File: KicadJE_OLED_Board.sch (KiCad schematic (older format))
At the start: 21 parts

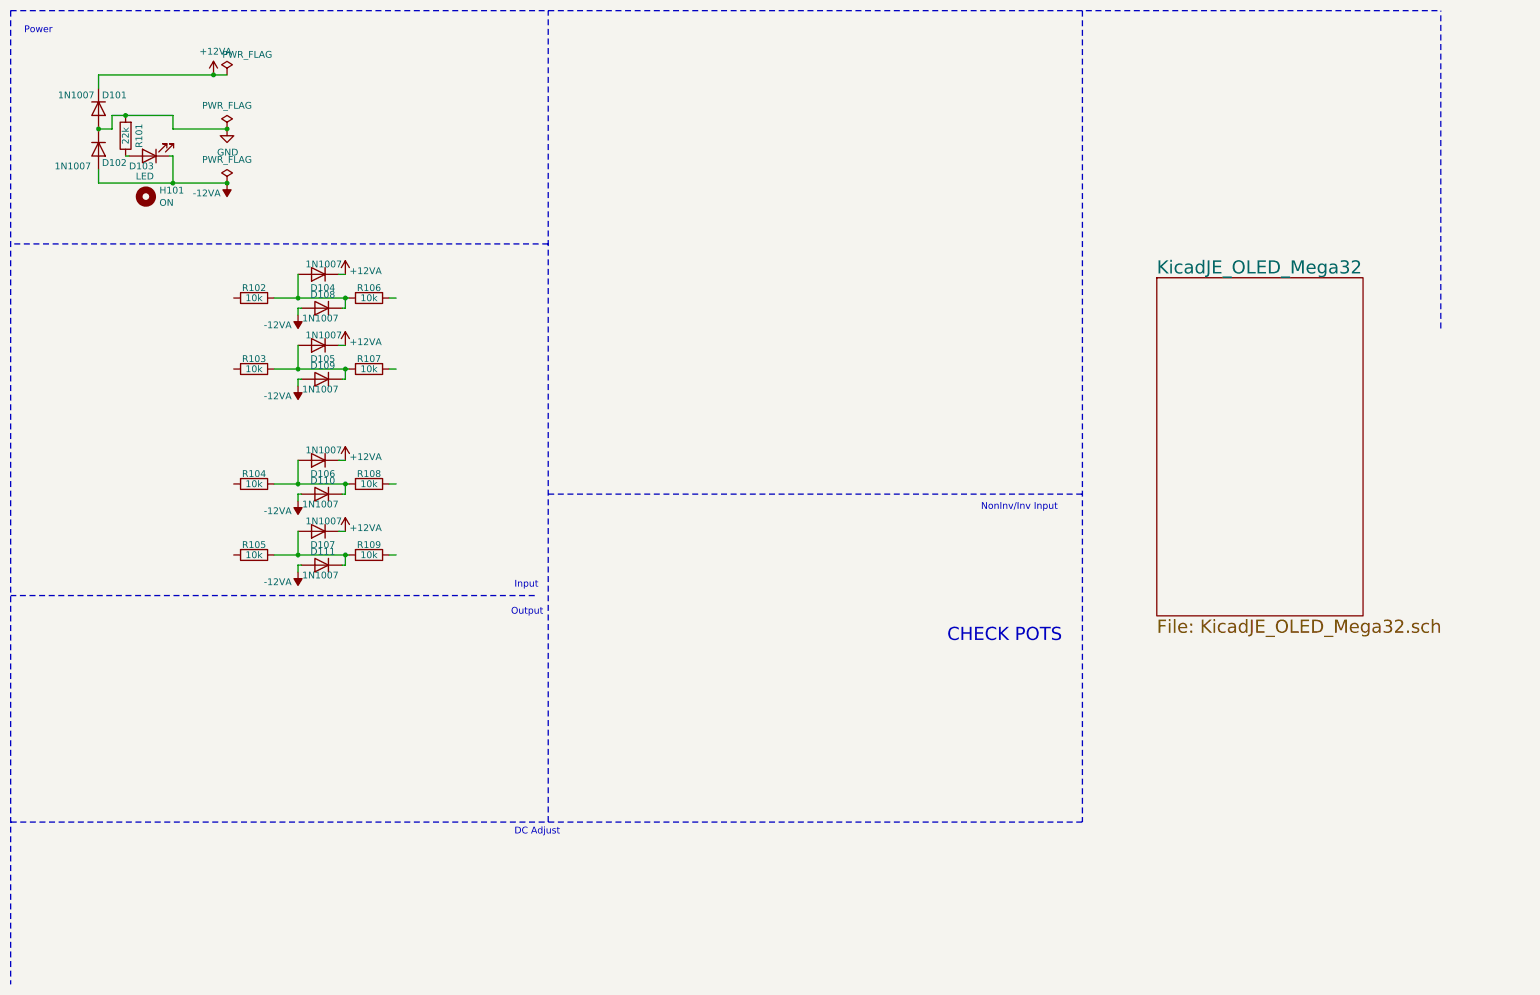
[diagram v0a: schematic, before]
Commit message: Small Amp/Filter circuit
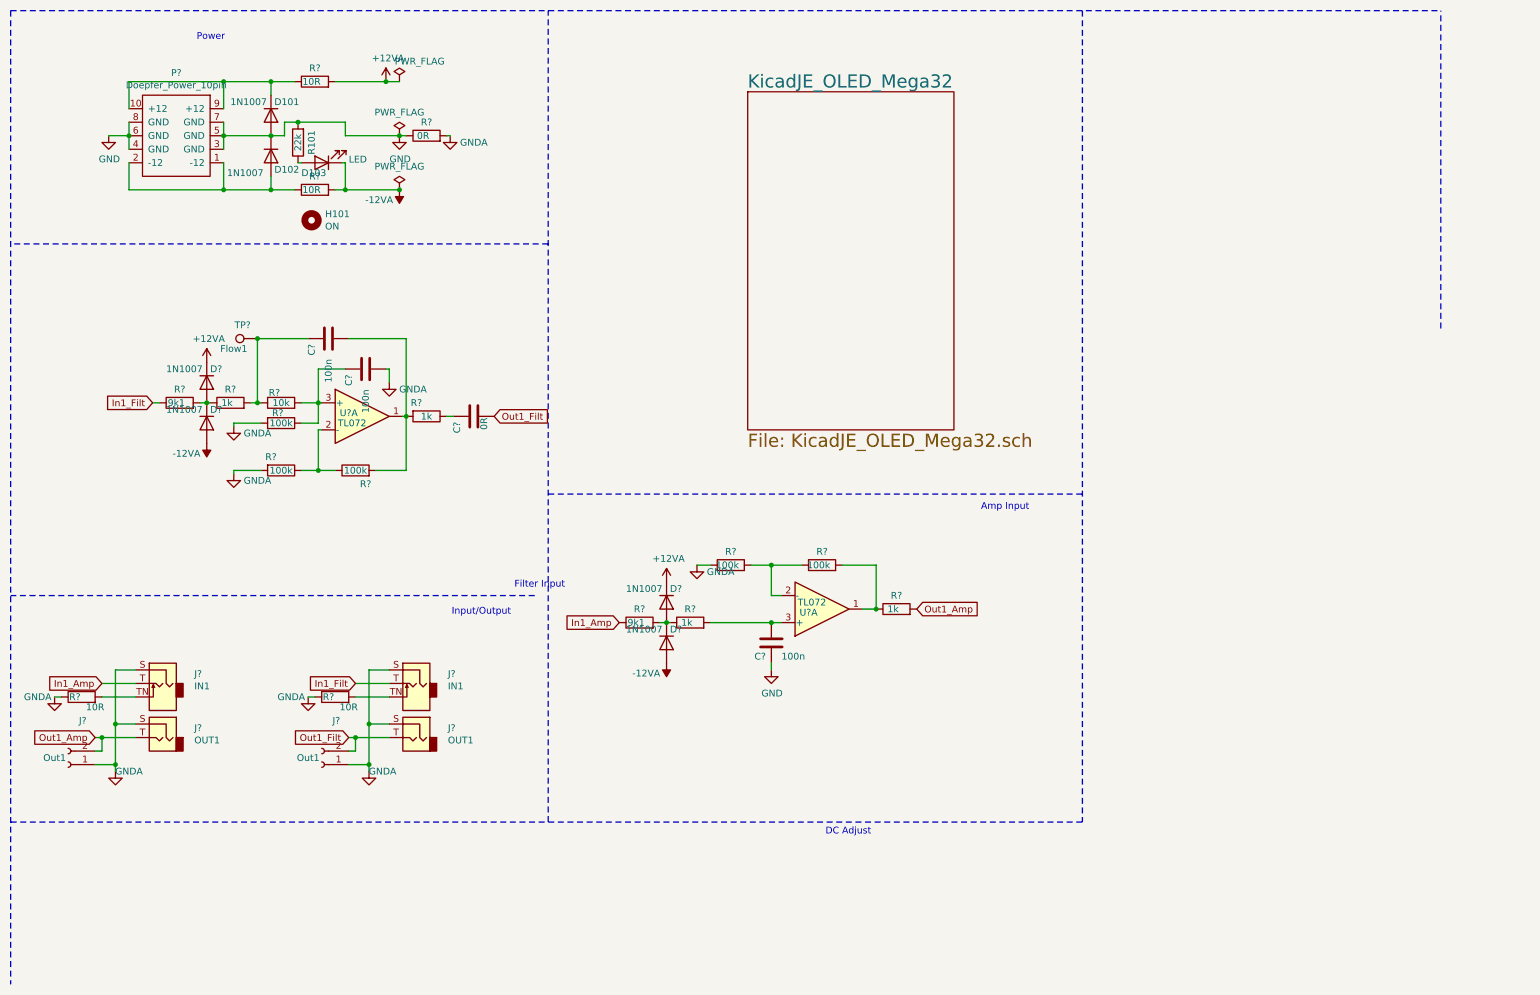
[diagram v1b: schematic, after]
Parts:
- removed D104, D105, D106, D107, D108, D109, D110, D111: 1N1007, AJ:D_SOD-123, symbol Device:D
- removed R102, R103, R104, R105, R106, R107, R108, R109: 10k, AJ:R_0805_AJ, symbol Device:R
- added C? (x3): 100n, AJ:C_0805_AJ, symbol Device:C
- added C?: 0R, AJ:C_0805_AJ, symbol Device:C
- added D? (x4): 1N1007, Diode_SMD:D_SOD-123, symbol Device:D
- added J? (x2): IN1, AJ:PJ301SM, symbol Connector:AudioJack2_SwitchT
- added J? (x2): OUT1, AJ:PJ301SM, symbol Connector:AudioJack2
- added J? (x2): Out1, Connector_PinSocket_2.54mm:PinSocket_1x02_P2.54mm_Vertical, symbol Connector:Conn_01x02_Female
- added P?: Doepfer_Power_10pin, Connectors_IDC:IDC-Header_2x05_Pitch2.54mm_Straight, symbol Eurorack:Doepfer_Power_10pin
- added R? (x4): 1k, AJ:R_0805_AJ, symbol Device:R
- added R? (x5): 100k, AJ:R_0805_AJ, symbol Device:R
- added R?: 10k, AJ:R_0805_AJ, symbol Device:R
- added R? (x4): 10R, AJ:R_0805_AJ, symbol Device:R
- added R? (x2): 9k1, AJ:R_0805_AJ, symbol Device:R
- added R?: 0R, AJ:R_0805_AJ, symbol Device:R
- added TP?: Flow1, TestPoint:TestPoint_THTPad_1.0x1.0mm_Drill0.5mm, symbol Connector:TestPoint
- added U? (x2): TL072, AJ:AJ_SO-8_5.3x6.2mm_P1.27mm, symbol Amplifier_Operational:TL072
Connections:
- net labels added: GNDA, In1_Amp, In1_Filt, Out1_Amp, Out1_Filt
- wire segments 55 -> 101
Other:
- note added: "Amp Input"
- note added: "Filter Input"
- note added: "Input/Output"
- note removed: "CHECK POTS"
- note removed: "Input"
- note removed: "NonInv/Inv Input"
- note removed: "Output"
- moved on the sheet: D101, D102, D103, H101, R101

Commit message: Update KicadJE_OLED_Board.sch
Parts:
- gave numbers to parts that had none: 35

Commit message: Update KicadJE_OLED_Board.sch
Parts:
- added C105, C106: 100n, AJ:C_0805_AJ, symbol Device:C
- added unit 3 of U101
- P101: footprint Connectors_IDC:IDC-Header_2x05_Pitch2.54mm_Straight -> Connector_IDC:IDC-Header_2x05_P2.54mm_Vertical
- renumbered U102 to U101
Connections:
- net +12VA: now also C105.1, U101.8 (V+)
- net -12VA: now also C106.2, U101.4 (V-)
- net GND: now also C105.2, C106.1
- net at R117.2, R118.1: now also U101.7; no longer U101.1
- net at R116.2, R117.1: now also U101.6 (-); no longer U101.2 (-)
- net at C104.1, R115.2: now also U101.5 (+); no longer U101.3 (+)
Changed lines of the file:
@@
 $EndComp
 Wire Wire Line
-	3000 1450 3400 1450
-Wire Wire Line
-	3000 1850 3400 1850
+	3000 1450 3175 1450
+Wire Wire Line
+	3000 1850 3175 1850
 Wire Wire Line
 	2450 1850 2625 1850
@@
 $Comp
 L Amplifier_Operational:TL072 U?
-U 1 1 6221EBDA
+U 2 1 6221EBDA
 P 6525 4950
 AR Path="/5D99B81E/6221EBDA" Ref="U?"  Part="3"
@@
 AR Path="/5E62ACA1/6221EBDA" Ref="U?"  Part="1"
 AR Path="/5F49A670/6221EBDA" Ref="U?"  Part="1"
-AR Path="/6221EBDA" Ref="U102"  Part="1"
+AR Path="/6221EBDA" Ref="U101"  Part="2"
 AR Path="/608CA457/6221EBDA" Ref="U?"  Part="2"
-F 0 "U102" H 6425 4975 50  0000 C CNN
+F 0 "U101" H 6425 4975 50  0000 C CNN
 F 1 "TL072" H 6450 4900 50  0000 C CNN
 F 2 "AJ:AJ_SO-8_5.3x6.2mm_P1.27mm" H 6525 4950 50  0001 C CNN
 F 3 "http://www.ti.com/lit/ds/symlink/tl071.pdf" H 6525 4950 50  0001 C CNN
-	1    6525 4950
+	2    6525 4950
 	1    0    0    1
 $EndComp
@@
 F 0 "P101" H 1750 985 50  0000 C CNN
 F 1 "Doepfer_Power_10pin" H 1750 1076 50  0000 C CNN
-F 2 "Connectors_IDC:IDC-Header_2x05_Pitch2.54mm_Straight" H 1750 1350 50  0001 C CNN
+F 2 "Connector_IDC:IDC-Header_2x05_P2.54mm_Vertical" H 1750 1350 50  0001 C CNN
 F 3 "DOCUMENTATION" H 1750 1350 50  0001 C CNN
 	1    1750 1350
@@
 $EndComp
 Wire Wire Line
-	2925 1050 3300 1050
+	2925 1050 3175 1050
 $Comp
 L Device:R R109
@@
 Wire Wire Line
 	2925 1850 3000 1850
+$Comp
+L Amplifier_Operational:TL072 U?
+U 3 1 6229AF2C
+P 4400 1450
+AR Path="/5D99B81E/6229AF2C" Ref="U?"  Part="3"
+AR Path="/5D99B7BA/6229AF2C" Ref="U?"  Part="1"
+AR Path="/5F18E4B5/6229AF2C" Ref="U?"  Part="2"
+AR Path="/5E62ACA1/6229AF2C" Ref="U?"  Part="1"
+AR Path="/5F49A670/6229AF2C" Ref="U?"  Part="1"
+AR Path="/6229AF2C" Ref="U101"  Part="3"
+AR Path="/608CA457/6229AF2C" Ref="U?"  Part="1"
+F 0 "U101" H 4300 1475 50  0000 C CNN
+F 1 "TL072" H 4325 1400 50  0000 C CNN
+F 2 "AJ:AJ_SO-8_5.3x6.2mm_P1.27mm" H 4400 1450 50  0001 C CNN
+F 3 "http://www.ti.com/lit/ds/symlink/tl071.pdf" H 4400 1450 50  0001 C CNN
+	3    4400 1450
+	1    0    0    -1
+$EndComp
+$Comp
+L power:+12VA #PWR0150
+U 1 1 6229EB47
+P 4300 1150
+F 0 "#PWR0150" H 4300 1000 50  0001 C CNN
+F 1 "+12VA" H 4315 1323 50  0000 C CNN
+F 2 "" H 4300 1150 50  0001 C CNN
+F 3 "" H 4300 1150 50  0001 C CNN
+	1    4300 1150
+	1    0    0    -1
+$EndComp
+$Comp
+L power:-12VA #PWR?
+U 1 1 6229EF55
+P 4300 1750
+AR Path="/5E4B0DD9/6229EF55" Ref="#PWR?"  Part="1"
+AR Path="/5E62ACA1/6229EF55" Ref="#PWR?"  Part="1"
+AR Path="/5F49A670/6229EF55" Ref="#PWR?"  Part="1"
+AR Path="/6229EF55" Ref="#PWR0151"  Part="1"
+F 0 "#PWR0151" H 4300 1600 50  0001 C CNN
+F 1 "-12VA" H 4450 1825 50  0000 C CNN
+F 2 "" H 4300 1750 50  0001 C CNN
+F 3 "" H 4300 1750 50  0001 C CNN
+	1    4300 1750
+	-1   0    0    1
+$EndComp
+$Comp
+L Device:C C106
+U 1 1 6229F3DC
+P 3175 1675
+AR Path="/6229F3DC" Ref="C106"  Part="1"
+AR Path="/5CD3F059/6229F3DC" Ref="C?"  Part="1"
+AR Path="/608CA457/6229F3DC" Ref="C?"  Part="1"
+F 0 "C106" H 3050 1800 50  0000 L CNN
+F 1 "100n" H 2850 1675 50  0000 L CNN
+F 2 "AJ:C_0805_AJ" H 3213 1525 50  0001 C CNN
+F 3 "~" H 3175 1675 50  0001 C CNN
+	1    3175 1675
+	1    0    0    -1
+$EndComp
+$Comp
+L Device:C C105
+U 1 1 6229F6F8
+P 3175 1250
+AR Path="/6229F6F8" Ref="C105"  Part="1"
+AR Path="/5CD3F059/6229F6F8" Ref="C?"  Part="1"
+AR Path="/608CA457/6229F6F8" Ref="C?"  Part="1"
+F 0 "C105" H 3050 1375 50  0000 L CNN
+F 1 "100n" H 2850 1250 50  0000 L CNN
+F 2 "AJ:C_0805_AJ" H 3213 1100 50  0001 C CNN
+F 3 "~" H 3175 1250 50  0001 C CNN
+	1    3175 1250
+	1    0    0    -1
+$EndComp
+Wire Wire Line
+	3175 1850 3175 1825
+Wire Wire Line
+	3175 1100 3175 1050
+Connection ~ 3175 1850
+Wire Wire Line
+	3175 1850 3400 1850
+Connection ~ 3175 1050
+Wire Wire Line
+	3175 1050 3300 1050
+Wire Wire Line
+	3175 1400 3175 1450
+Connection ~ 3175 1450
+Wire Wire Line
+	3175 1450 3400 1450
+Wire Wire Line
+	3175 1450 3175 1525
 $EndSCHEMATC

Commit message: Filt/Amp Netlist
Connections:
- net InNeg: now reaches D102.2 (A), P101.1 (-12), P101.2 (-12), R109.1
- net InPos: now reaches D101.1 (K), P101.10 (+12), P101.9 (+12), R108.1
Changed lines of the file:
@@
 Wire Wire Line
 	3175 1450 3175 1525
+Text Label 1400 1050 0    97   ~ 0
+InPos
+Text Label 1400 1850 0    97   ~ 0
+InNeg
 $EndSCHEMATC

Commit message: Amp/Filt
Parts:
- added J107: In1, Connector_PinSocket_2.54mm:PinSocket_1x02_P2.54mm_Vertical, symbol Connector:Conn_01x02_Female
- added J108: InFlt, Connector_PinSocket_2.54mm:PinSocket_1x02_P2.54mm_Vertical, symbol Connector:Conn_01x02_Female
- added TP?: AmpOut1, TestPoint:TestPoint_THTPad_1.0x1.0mm_Drill0.5mm, symbol Connector:TestPoint
- J104: value Out1 -> OutFlt
- J105: value IN1 -> INFLT
- J106: value OUT1 -> OUTFLT
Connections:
- net GNDA: now also J107.1 (Pin_1), J108.1 (Pin_1)
- net In1_Amp: now also J107.2 (Pin_2)
- net In1_Filt: now also J108.2 (Pin_2)
- net at R117.2, R118.1, U101.7: now also TP?.1
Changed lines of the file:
@@
 AR Path="/608CA457/6222A282" Ref="J?"  Part="1"
 F 0 "J105" H 3292 5571 50  0000 R CNN
-F 1 "IN1" H 3292 5480 50  0000 R CNN
+F 1 "INFLT" H 3292 5480 50  0000 R CNN
 F 2 "AJ:PJ301SM" H 3525 5500 50  0001 C CNN
 F 3 "~" H 3525 5500 50  0001 C CNN
@@
 $EndComp
 Wire Wire Line
-	3075 5500 3325 5500
+	3075 5500 3225 5500
 Wire Wire Line
 	3325 5400 3175 5400
@@
 AR Path="/608CA457/6222A29C" Ref="J?"  Part="1"
 F 0 "J106" H 3292 5971 50  0000 R CNN
-F 1 "OUT1" H 3292 5880 50  0000 R CNN
+F 1 "OUTFLT" H 3292 5880 50  0000 R CNN
 F 2 "AJ:PJ301SM" H 3525 5900 50  0001 C CNN
 F 3 "~" H 3525 5900 50  0001 C CNN
@@
 AR Path="/6222A2B8" Ref="J104"  Part="1"
 F 0 "J104" H 2717 5775 50  0000 C CNN
-F 1 "Out1" H 2925 6050 50  0000 C CNN
+F 1 "OutFlt" H 2925 6050 50  0000 C CNN
 F 2 "Connector_PinSocket_2.54mm:PinSocket_1x02_P2.54mm_Vertical" H 2825 6100 50  0001 C CNN
 F 3 "~" H 2825 6100 50  0001 C CNN
@@
 $EndComp
 Wire Wire Line
-	1200 5500 1450 5500
+	1200 5500 1375 5500
 Wire Wire Line
 	1450 5400 1300 5400
@@
 Text Label 1400 1850 0    97   ~ 0
 InNeg
+$Comp
+L Connector:Conn_01x02_Female J?
+U 1 1 622BC023
+P 2975 5400
+AR Path="/608CA457/622BC023" Ref="J?"  Part="1"
+AR Path="/622BC023" Ref="J108"  Part="1"
+F 0 "J108" H 2867 5075 50  0000 C CNN
+F 1 "InFlt" H 3075 5350 50  0000 C CNN
+F 2 "Connector_PinSocket_2.54mm:PinSocket_1x02_P2.54mm_Vertical" H 2975 5400 50  0001 C CNN
+F 3 "~" H 2975 5400 50  0001 C CNN
+	1    2975 5400
+	-1   0    0    1
+$EndComp
+Connection ~ 3175 5400
+Wire Wire Line
+	3175 5300 3225 5300
+Wire Wire Line
+	3225 5300 3225 5500
+Connection ~ 3225 5500
+Wire Wire Line
+	3225 5500 3325 5500
+$Comp
+L Connector:Conn_01x02_Female J?
+U 1 1 622C128F
+P 1100 5400
+AR Path="/608CA457/622C128F" Ref="J?"  Part="1"
+AR Path="/622C128F" Ref="J107"  Part="1"
+F 0 "J107" H 992 5075 50  0000 C CNN
+F 1 "In1" H 1200 5350 50  0000 C CNN
+F 2 "Connector_PinSocket_2.54mm:PinSocket_1x02_P2.54mm_Vertical" H 1100 5400 50  0001 C CNN
+F 3 "~" H 1100 5400 50  0001 C CNN
+	1    1100 5400
+	-1   0    0    1
+$EndComp
+Connection ~ 1300 5400
+Wire Wire Line
+	1300 5300 1375 5300
+Wire Wire Line
+	1375 5300 1375 5500
+Connection ~ 1375 5500
+Wire Wire Line
+	1375 5500 1450 5500
+$Comp
+L Connector:TestPoint TP?
+U 1 1 622EAFCD
+P 6925 4950
+AR Path="/622EAFCD" Ref="TP?"  Part="1"
+AR Path="/608CA457/622EAFCD" Ref="TP?"  Part="1"
+F 0 "TP?" V 7025 5000 50  0000 L CNN
+F 1 "AmpOut1" V 6850 5025 50  0000 L CNN
+F 2 "TestPoint:TestPoint_THTPad_1.0x1.0mm_Drill0.5mm" H 7125 4950 50  0001 C CNN
+F 3 "~" H 7125 4950 50  0001 C CNN
+	1    6925 4950
+	-1   0    0    1
+$EndComp
 $EndSCHEMATC

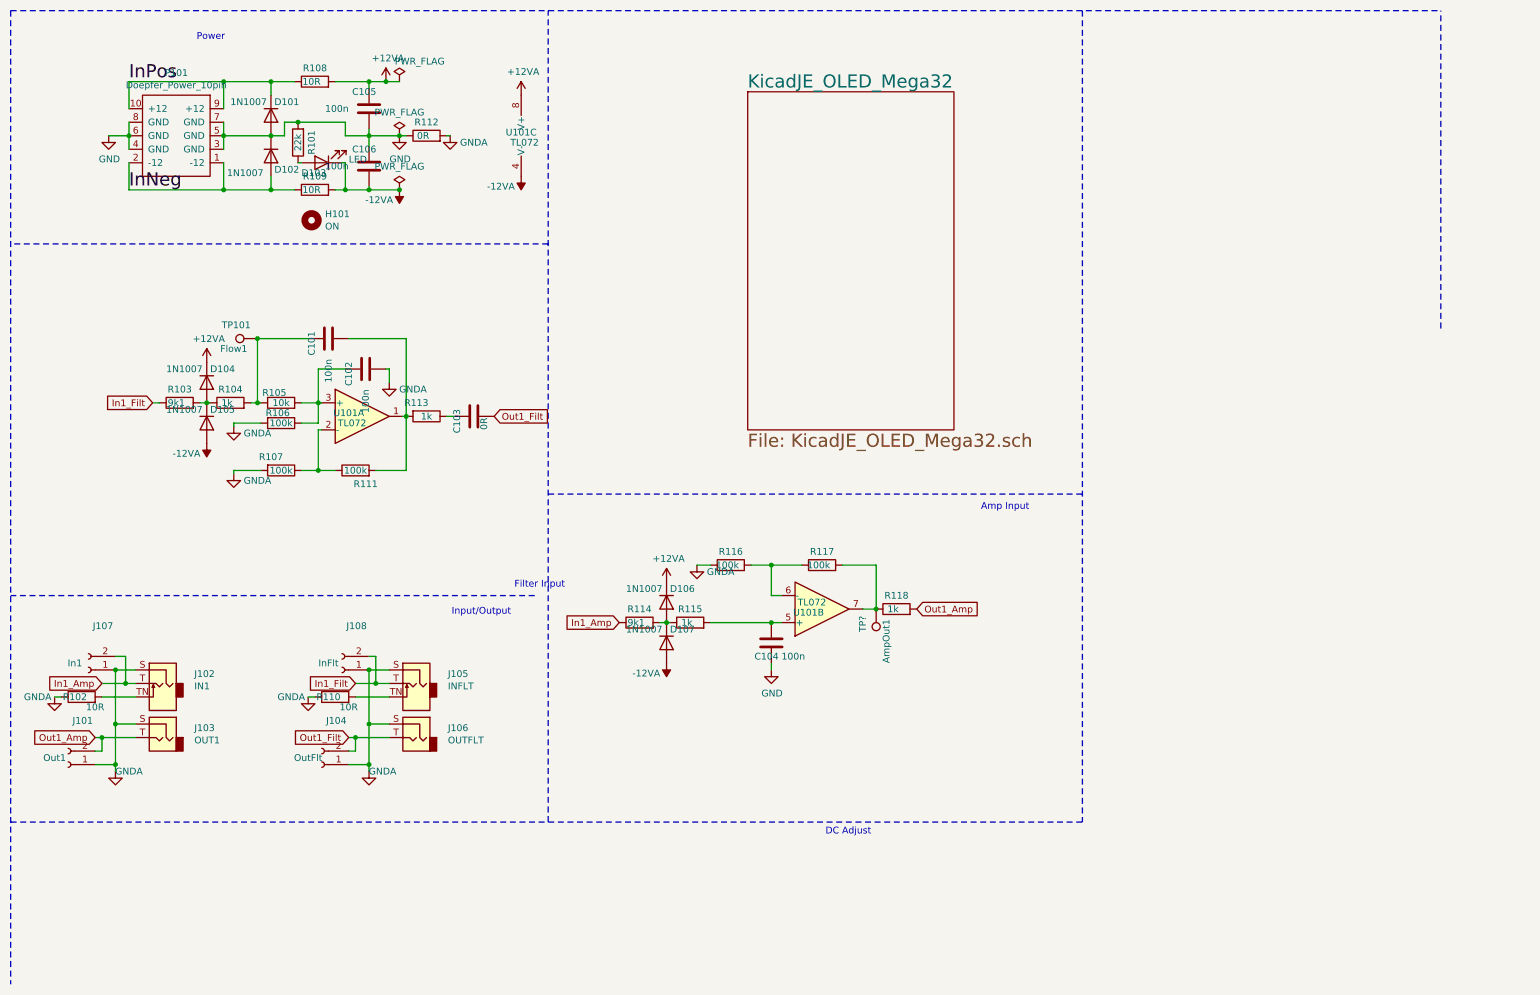
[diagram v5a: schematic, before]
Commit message: move pinhdr from in jacks to input circuit
after protection resistor - so pcb may be cut above the connectors in case this is needed
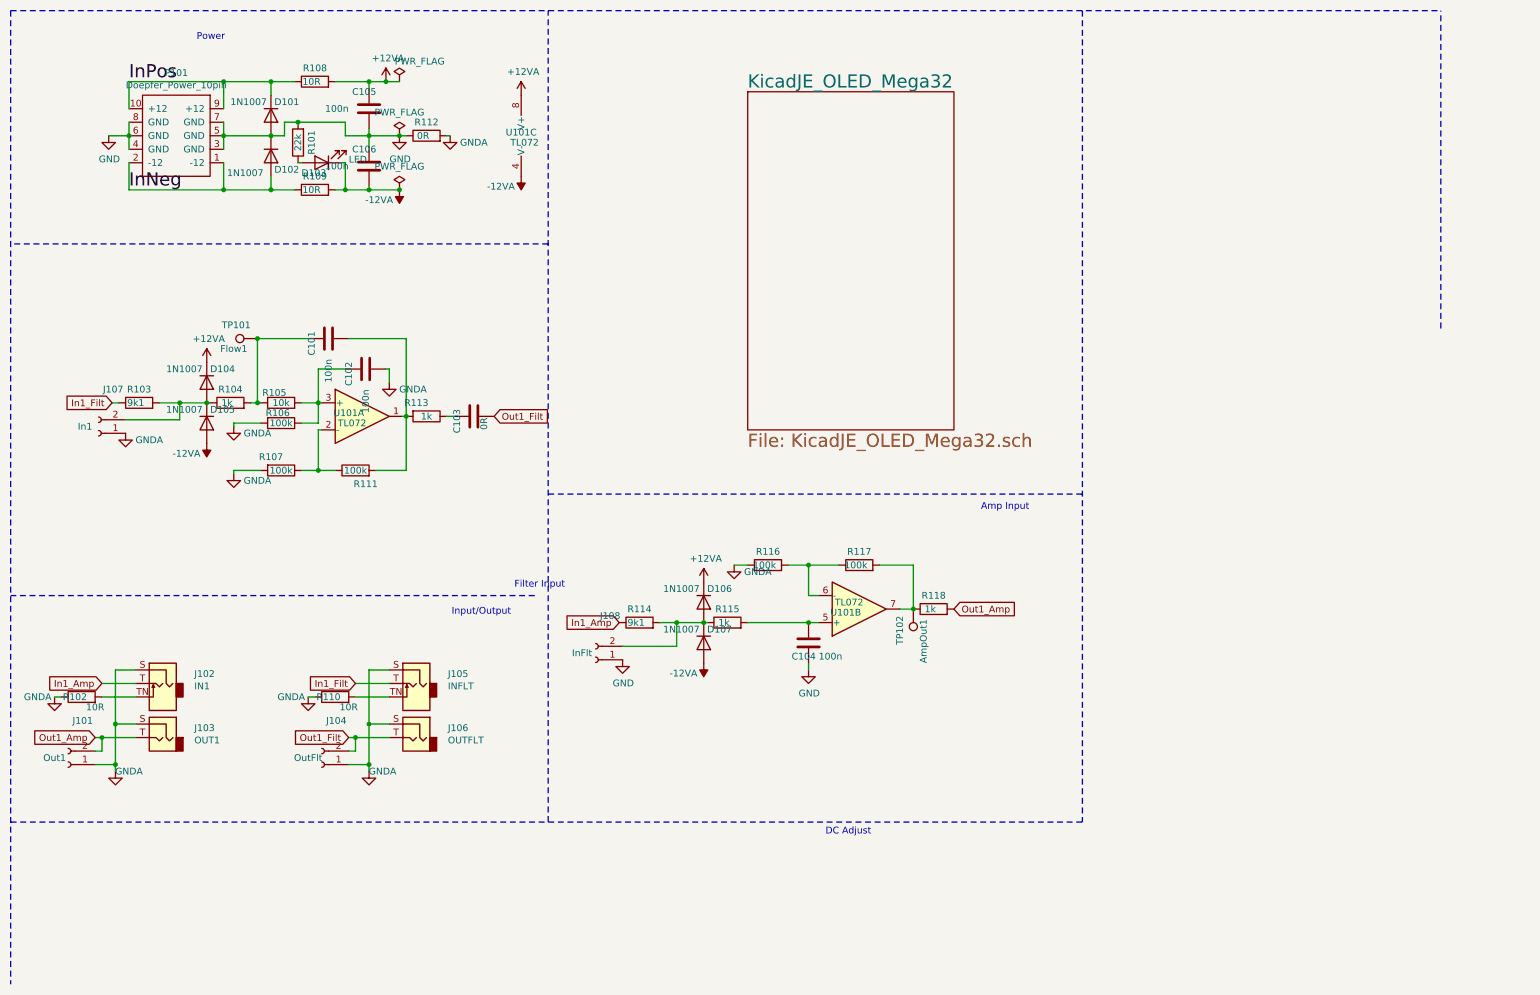
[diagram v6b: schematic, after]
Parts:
- removed H101: ON, AJ:LED_Hole_3mm, symbol Mechanical:MountingHole
- D103: footprint AJ:D_SOD-123 -> AJ:D_0805_AJ
- gave numbers to parts that had none: 1
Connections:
- net GND: now also J108.1 (Pin_1)
- net GNDA: no longer J108.1 (Pin_1)
- net In1_Amp: no longer J107.2 (Pin_2)
- net In1_Filt: no longer J108.2 (Pin_2)
- net at D104.2 (A), D105.1 (K), R103.2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: now also J107.2 (Pin_2)
- net at D106.2 (A), D107.1 (K), R114.2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: now also J108.2 (Pin_2)
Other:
- moved on the sheet: C104, D106, D107, J107, J108, R103, R115, R116, R117, R118, TP102, U101B
